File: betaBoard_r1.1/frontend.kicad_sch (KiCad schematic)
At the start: 16 parts, among them U5 LM358

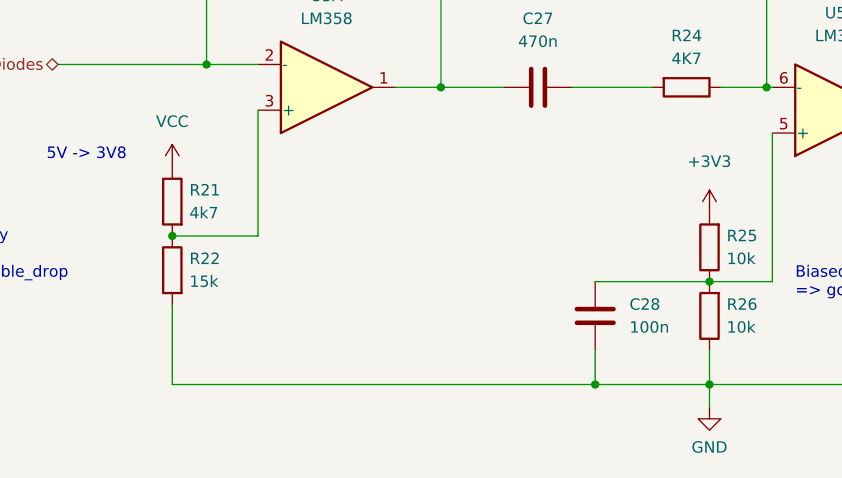
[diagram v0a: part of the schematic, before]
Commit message: move all hardware files to one folder
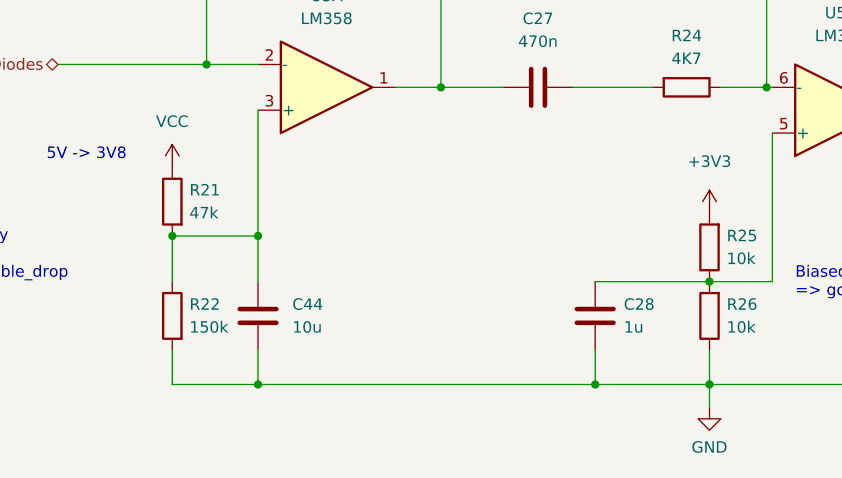
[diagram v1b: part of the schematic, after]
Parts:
- added C44: 10u, Capacitor_SMD:C_0603_1608Metric, symbol Device:C
- C28: value 100n -> 1u
- R21: value 4k7 -> 47k
- R22: value 15k -> 150k
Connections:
- net GND: now also C44.2
- net at R21.2, R22.1, U5.3 (+): now also C44.1
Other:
- moved on the sheet: R22
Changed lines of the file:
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@@
     (title "Beta Board")
     (date "2023-12-28")
-    (rev "R1.0")
+    (rev "R1.1")
     (company "Tim Kuhlbusch")
     (comment 1 "Beta radiation detector")
@@
   (junction (at 155.575 136.525) (diameter 0) (color 0 0 0 0)
   )
+  (junction (at 105.41 120.015) (diameter 0) (color 0 0 0 0)
+  )
   (junction (at 204.47 106.045) (diameter 0) (color 0 0 0 0)
   )
   (junction (at 95.885 120.015) (diameter 0) (color 0 0 0 0)
   )
+  (junction (at 105.41 136.525) (diameter 0) (color 0 0 0 0)
+  )
   (junction (at 125.73 103.505) (diameter 0) (color 0 0 0 0)
   )
@@
     (stroke (width 0) (type default))
   )
+  (wire (pts (xy 105.41 125.095) (xy 105.41 120.015))
+    (stroke (width 0) (type default))
+  )
   (wire (pts (xy 162.56 125.095) (xy 162.56 108.585))
     (stroke (width 0) (type default))
@@
     (stroke (width 0) (type default))
   )
+  (wire (pts (xy 95.885 125.095) (xy 95.885 120.015))
+    (stroke (width 0) (type default))
+  )
   (wire (pts (xy 155.575 125.095) (xy 162.56 125.095))
     (stroke (width 0) (type default))
@@
     (stroke (width 0) (type default))
   )
+  (wire (pts (xy 105.41 132.715) (xy 105.41 136.525))
+    (stroke (width 0) (type default))
+  )
   (wire (pts (xy 167.005 90.17) (xy 161.925 90.17))
     (stroke (width 0) (type default))
@@
     (stroke (width 0) (type default))
   )
+  (wire (pts (xy 105.41 136.525) (xy 95.885 136.525))
+    (stroke (width 0) (type default))
+  )
   (wire (pts (xy 155.575 136.525) (xy 204.47 136.525))
     (stroke (width 0) (type default))
@@
     (stroke (width 0) (type default))
   )
-  (wire (pts (xy 142.875 136.525) (xy 95.885 136.525))
+  (wire (pts (xy 142.875 136.525) (xy 105.41 136.525))
     (stroke (width 0) (type default))
   )
@@
     (stroke (width 0) (type default))
   )
-  (wire (pts (xy 95.885 136.525) (xy 95.885 127.635))
+  (wire (pts (xy 95.885 136.525) (xy 95.885 132.715))
     (stroke (width 0) (type default))
   )
@@
   (symbol (lib_id "Device:R") (at 95.885 116.205 0) (mirror y) (unit 1)
     (in_bom yes) (on_board yes) (dnp no) (fields_autoplaced)
-    (property "Reference" "R21" (at 97.79 114.9349 0)
+    (property "Reference" "R21" (at 97.79 114.935 0)
       (effects (font (size 1.27 1.27)) (justify right))
     )
-    (property "Value" "4k7" (at 97.79 117.4749 0)
+    (property "Value" "47k" (at 97.79 117.475 0)
       (effects (font (size 1.27 1.27)) (justify right))
     )
@@
     )
   )
-  (symbol (lib_id "Device:R") (at 95.885 123.825 0) (mirror y) (unit 1)
-    (in_bom yes) (on_board yes) (dnp no) (fields_autoplaced)
-    (property "Reference" "R22" (at 97.79 122.5549 0)
+  (symbol (lib_id "Device:R") (at 95.885 128.905 0) (mirror y) (unit 1)
+    (in_bom yes) (on_board yes) (dnp no) (fields_autoplaced)
+    (property "Reference" "R22" (at 97.79 127.635 0)
       (effects (font (size 1.27 1.27)) (justify right))
     )
-    (property "Value" "15k" (at 97.79 125.0949 0)
+    (property "Value" "150k" (at 97.79 130.175 0)
       (effects (font (size 1.27 1.27)) (justify right))
     )
-    (property "Footprint" "Resistor_SMD:R_0603_1608Metric" (at 97.663 123.825 90)
-      (effects (font (size 1.27 1.27)) hide)
-    )
-    (property "Datasheet" "~" (at 95.885 123.825 0)
+    (property "Footprint" "Resistor_SMD:R_0603_1608Metric" (at 97.663 128.905 90)
+      (effects (font (size 1.27 1.27)) hide)
+    )
+    (property "Datasheet" "~" (at 95.885 128.905 0)
       (effects (font (size 1.27 1.27)) hide)
     )
@@
     )
   )
+  (symbol (lib_id "Device:C") (at 105.41 128.905 0) (unit 1)
+    (in_bom yes) (on_board yes) (dnp no) (fields_autoplaced)
+    (property "Reference" "C44" (at 109.22 127.635 0)
+      (effects (font (size 1.27 1.27)) (justify left))
+    )
+    (property "Value" "10u" (at 109.22 130.175 0)
+      (effects (font (size 1.27 1.27)) (justify left))
+    )
+    (property "Footprint" "Capacitor_SMD:C_0603_1608Metric" (at 106.3752 132.715 0)
+      (effects (font (size 1.27 1.27)) hide)
+    )
+    (property "Datasheet" "~" (at 105.41 128.905 0)
+      (effects (font (size 1.27 1.27)) hide)
+    )
+    (pin "1")
+    (pin "2")
+    (instances
+      (project "betaBoard"
+        (path "/3d37b943-9a24-43ad-9fbf-b901b38695ce/1d31b165-afd9-4178-8caf-a7fc7b259f97"
+          (reference "C44") (unit 1)
+        )
+        (path "/3d37b943-9a24-43ad-9fbf-b901b38695ce/a19c94be-85f2-45d0-b8ae-fe772296c136"
+          (reference "C45") (unit 1)
+        )
+        (path "/3d37b943-9a24-43ad-9fbf-b901b38695ce/cd42d678-88a0-4889-b461-e4aa141e3c58"
+          (reference "C46") (unit 1)
+        )
+        (path "/3d37b943-9a24-43ad-9fbf-b901b38695ce/617ca541-d0cd-4a41-a58b-d194673edcc6"
+          (reference "C47") (unit 1)
+        )
+      )
+    )
+  )
   (symbol (lib_id "Device:R") (at 155.575 128.905 180) (unit 1)
     (in_bom yes) (on_board yes) (dnp no) (fields_autoplaced)
@@
   (symbol (lib_id "Device:C") (at 142.875 128.905 0) (unit 1)
     (in_bom yes) (on_board yes) (dnp no) (fields_autoplaced)
-    (property "Reference" "C28" (at 146.685 127.6349 0)
+    (property "Reference" "C28" (at 146.05 127.635 0)
       (effects (font (size 1.27 1.27)) (justify left))
     )
-    (property "Value" "100n" (at 146.685 130.1749 0)
+    (property "Value" "1u" (at 146.05 130.175 0)
       (effects (font (size 1.27 1.27)) (justify left))
     )
